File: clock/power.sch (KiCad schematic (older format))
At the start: 50 parts, among them Q501 BSS138, Q502 BSS138, U501 TPS56428, U502 TPS56428, U503 TPS56428

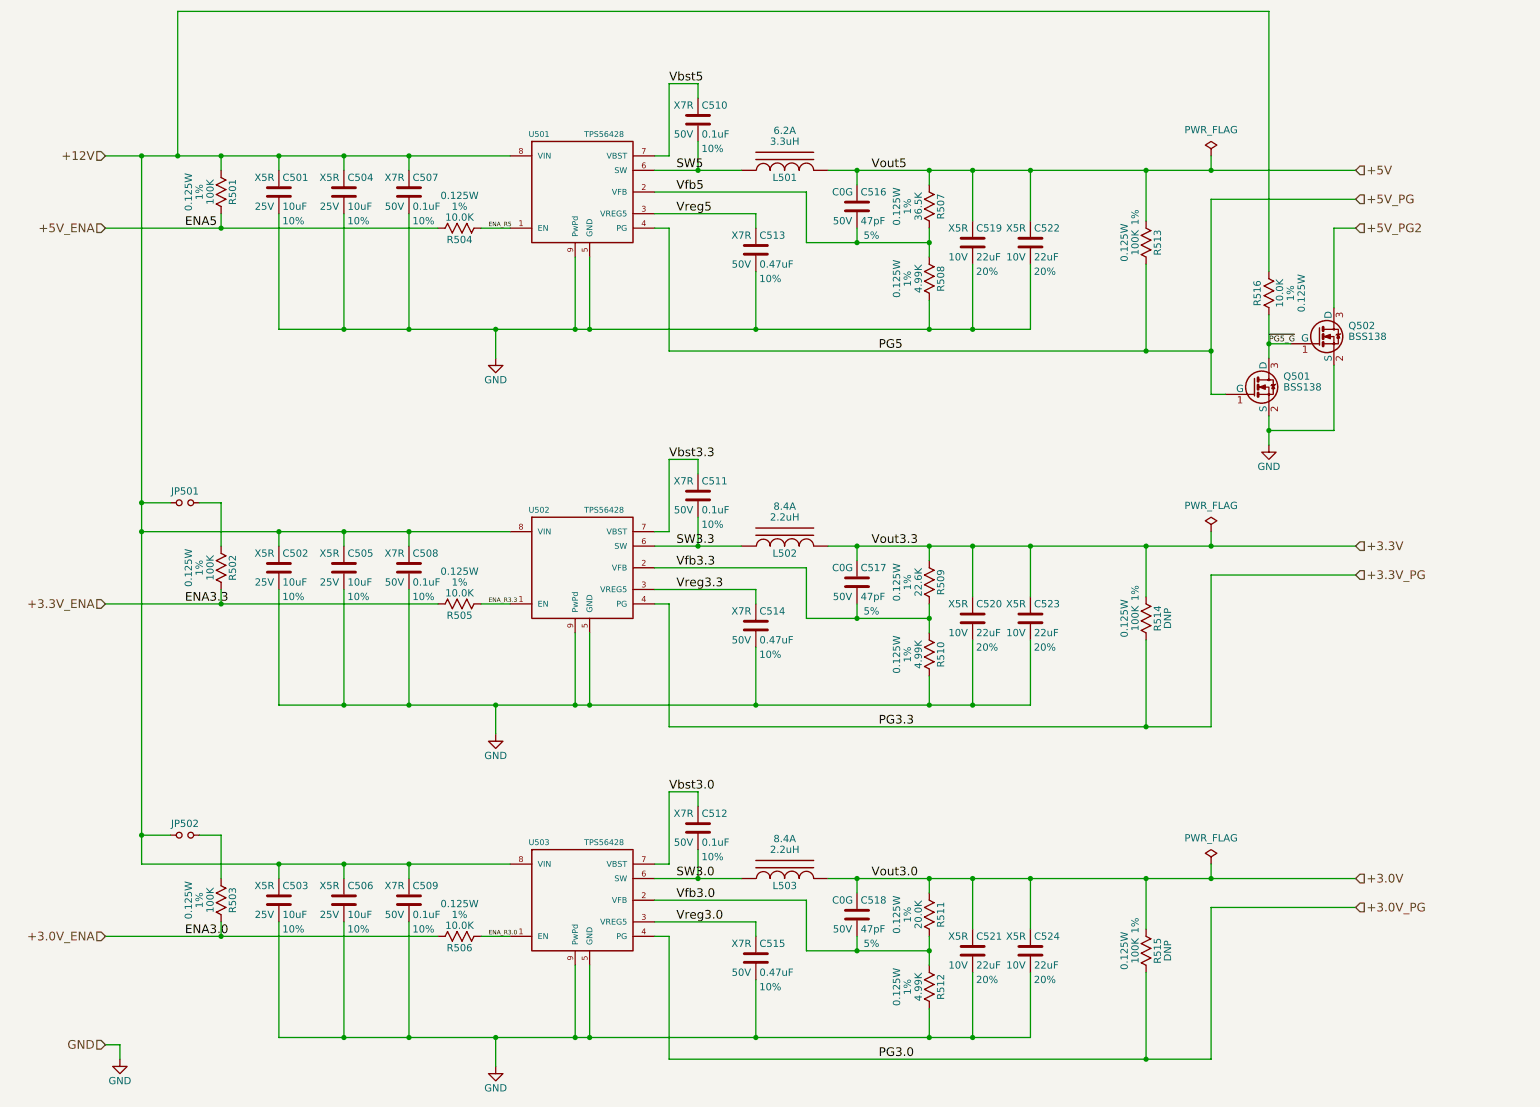
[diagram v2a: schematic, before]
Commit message: Add power indication LEDs.
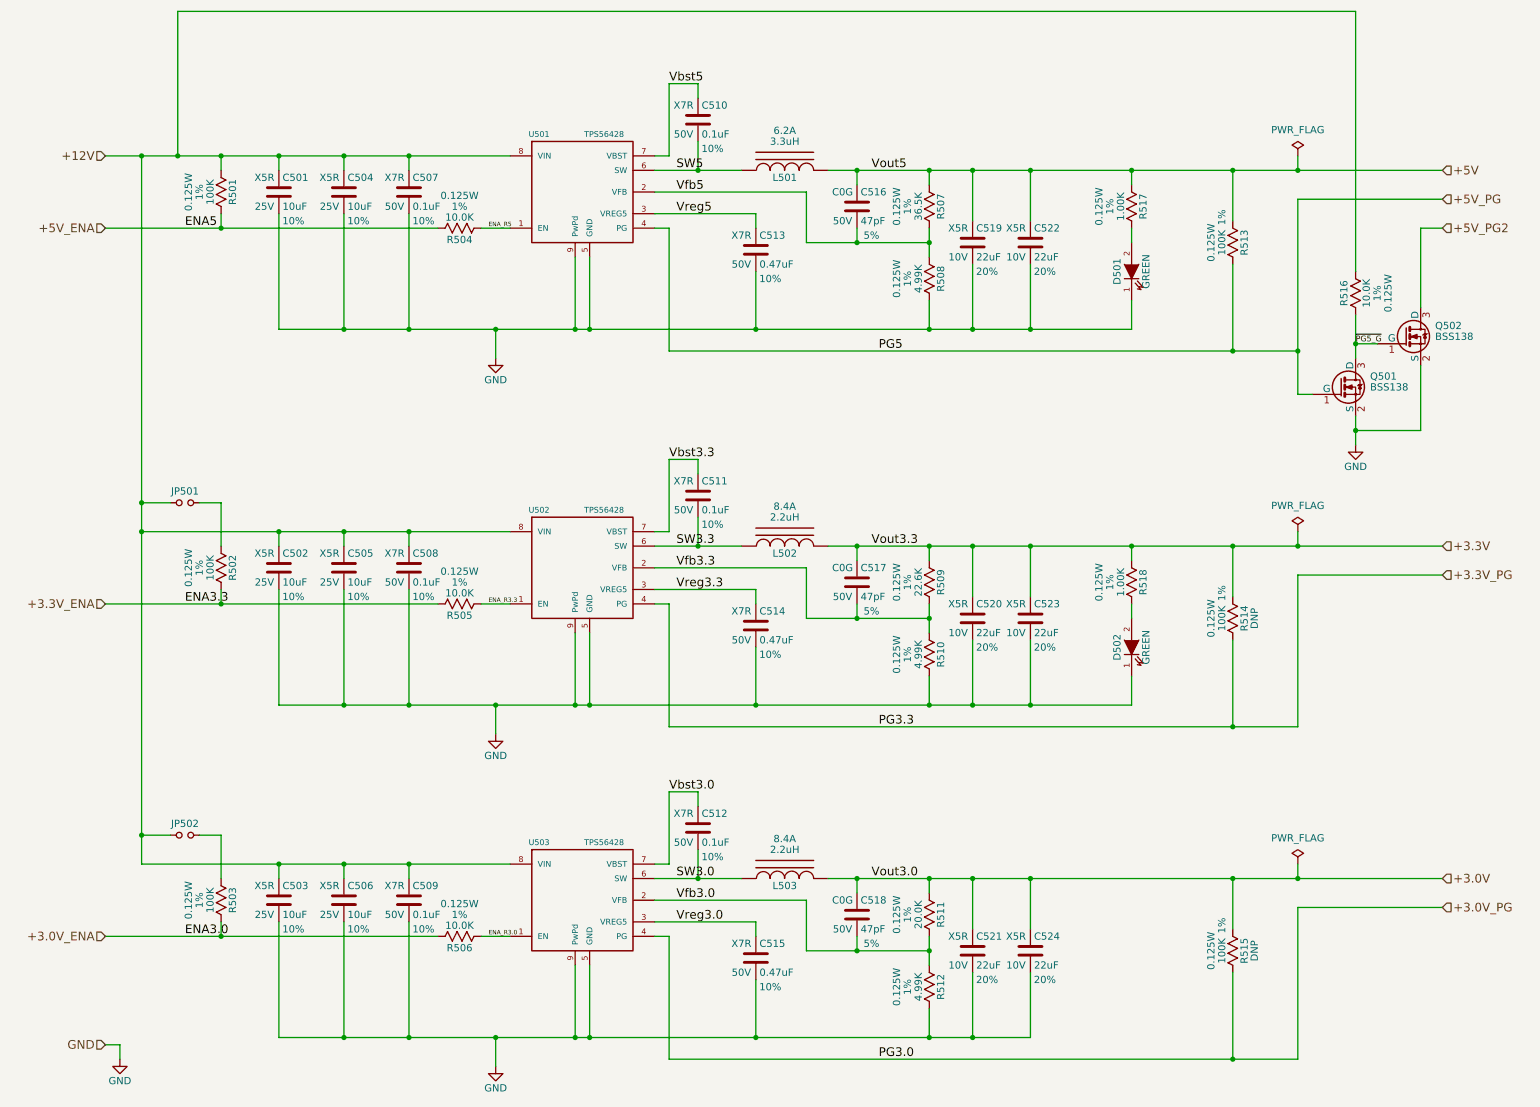
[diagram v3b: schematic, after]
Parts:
- added D501, D502: GREEN, local:LED_0805_HandSoldering, symbol LED
- added R517, R518: 1.00K, local:R_0805_HandSoldering, symbol R_local
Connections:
- net +3.3V: now also R518.1
- net +5V: now also R517.1
- net GND: now also D501.1 (K), D502.1 (K)
- new net: D501.2 (A), R517.2
- new net: D502.2 (A), R518.2
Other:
- moved on the sheet: Q501, Q502, R513, R514, R515, R516

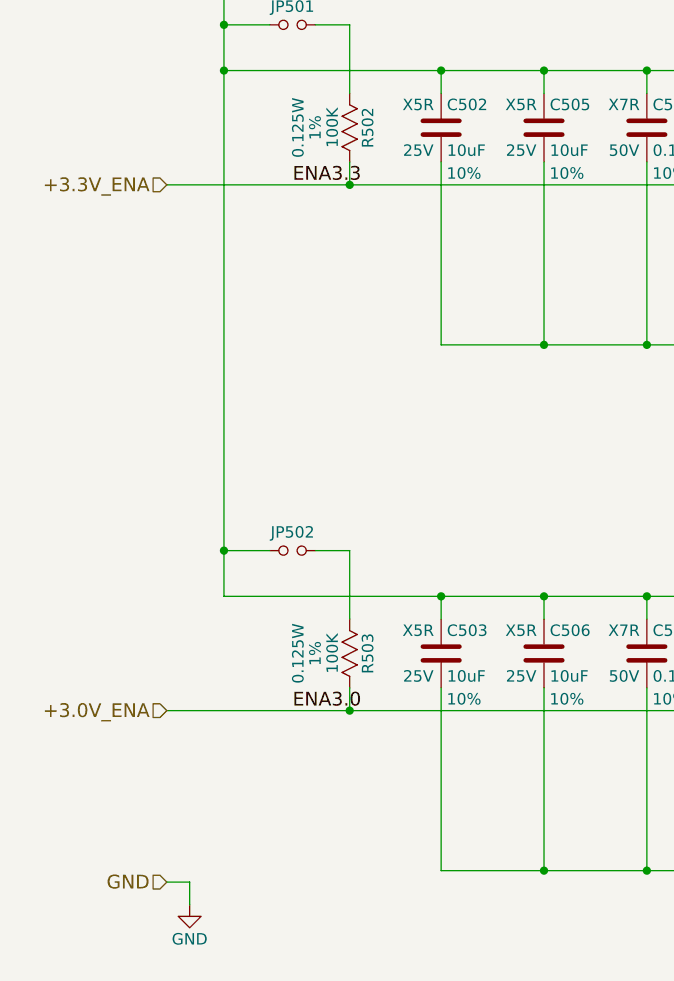
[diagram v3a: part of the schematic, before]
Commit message: Remove sheet to sheet power interconnect because power symbols are global.
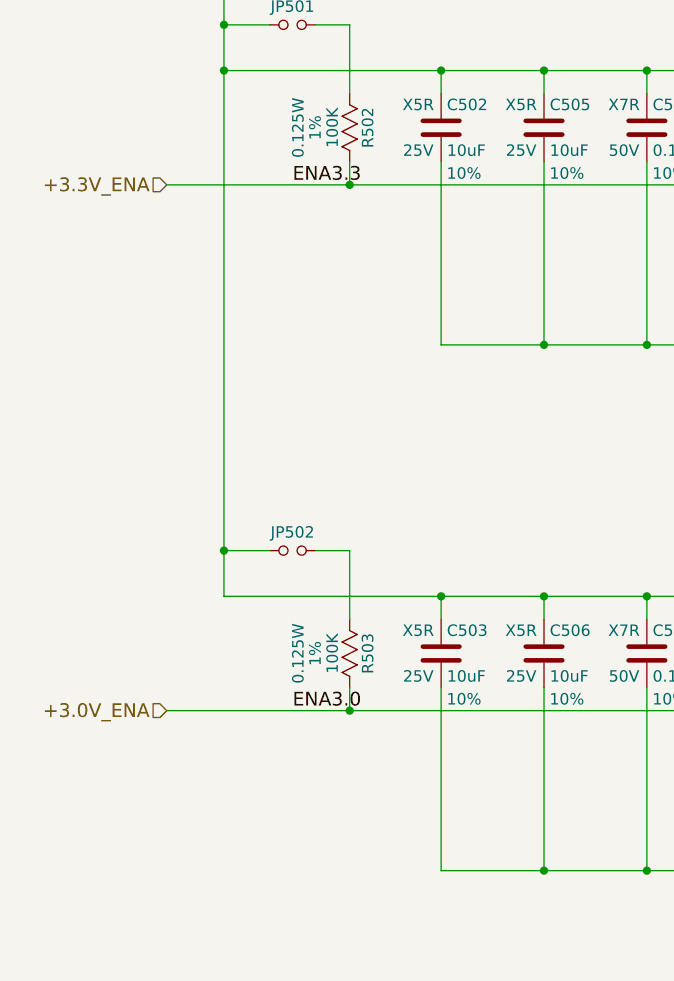
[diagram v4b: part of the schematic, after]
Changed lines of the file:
@@
 Connection ~ 4300 2750
 $Comp
-L GND #PWR502
+L GND #PWR074
 U 1 1 55FF67B4
 P 6200 3650
-F 0 "#PWR502" H 6200 3400 50  0001 C CNN
+F 0 "#PWR074" H 6200 3400 50  0001 C CNN
 F 1 "GND" H 6200 3500 50  0000 C CNN
 F 2 "" H 6200 3650 60  0000 C CNN
@@
 Connection ~ 5150 6050
 Wire Wire Line
-	4700 5250 4700 6050
+	4700 6050 4700 5250
 Wire Wire Line
 	4700 4950 4700 4850
@@
 Connection ~ 4300 5350
 $Comp
-L GND #PWR503
+L GND #PWR075
 U 1 1 5619E4B9
 P 6200 6250
-F 0 "#PWR503" H 6200 6000 50  0001 C CNN
+F 0 "#PWR075" H 6200 6000 50  0001 C CNN
 F 1 "GND" H 6200 6100 50  0000 C CNN
 F 2 "" H 6200 6250 60  0000 C CNN
@@
 Connection ~ 4300 7650
 $Comp
-L GND #PWR504
+L GND #PWR076
 U 1 1 561A0FCA
 P 6200 8550
-F 0 "#PWR504" H 6200 8300 50  0001 C CNN
+F 0 "#PWR076" H 6200 8300 50  0001 C CNN
 F 1 "GND" H 6200 8400 50  0000 C CNN
 F 2 "" H 6200 8550 60  0000 C CNN
@@
 	3950 6950 3750 6950
 Connection ~ 3750 6950
-Text HLabel 3500 8400 0    60   Input ~ 0
-GND
-$Comp
-L GND #PWR501
-U 1 1 563D8E93
-P 3600 8500
-F 0 "#PWR501" H 3600 8250 50  0001 C CNN
-F 1 "GND" H 3600 8350 50  0000 C CNN
-F 2 "" H 3600 8500 60  0000 C CNN
-F 3 "" H 3600 8500 60  0000 C CNN
-	1    3600 8500
-	1    0    0    -1
-$EndComp
-Wire Wire Line
-	3600 8400 3600 8500
-Wire Wire Line
-	3600 8400 3500 8400
-$Comp
-L PWR_FLAG #FLG501
+$Comp
+L PWR_FLAG #FLG077
 U 1 1 56439BF3
 P 11750 2250
-F 0 "#FLG501" H 11750 2345 50  0001 C CNN
+F 0 "#FLG077" H 11750 2345 50  0001 C CNN
 F 1 "PWR_FLAG" H 11750 2430 50  0000 C CNN
 F 2 "" H 11750 2250 60  0000 C CNN
@@
 Connection ~ 11750 2350
 $Comp
-L PWR_FLAG #FLG502
+L PWR_FLAG #FLG078
 U 1 1 5643A4B3
 P 11750 4850
-F 0 "#FLG502" H 11750 4945 50  0001 C CNN
+F 0 "#FLG078" H 11750 4945 50  0001 C CNN
 F 1 "PWR_FLAG" H 11750 5030 50  0000 C CNN
 F 2 "" H 11750 4850 60  0000 C CNN
@@
 Connection ~ 11750 4950
 $Comp
-L PWR_FLAG #FLG503
+L PWR_FLAG #FLG079
 U 1 1 5643AC28
 P 11750 7150
-F 0 "#FLG503" H 11750 7245 50  0001 C CNN
+F 0 "#FLG079" H 11750 7245 50  0001 C CNN
 F 1 "PWR_FLAG" H 11750 7330 50  0000 C CNN
 F 2 "" H 11750 7150 60  0000 C CNN
@@
 	12150 4050 12150 4250
 $Comp
-L GND #PWR505
+L GND #PWR080
 U 1 1 57A97EAC
 P 12150 4250
-F 0 "#PWR505" H 12150 4000 50  0001 C CNN
+F 0 "#PWR080" H 12150 4000 50  0001 C CNN
 F 1 "GND" H 12150 4100 50  0000 C CNN
 F 2 "" H 12150 4250 60  0000 C CNN

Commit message: Update clock board to kicad 5.1. Regenerate output files.
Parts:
- C501, C502, C503, C504, C505, C506, C507, C508, C509, C510, C511, C512, C513, C514, C515, C516, C517, C518, C519, C520, C521, C522, C523, C524: symbol C -> Device:C
- D501, D502: symbol LED -> Local:LED
- JP501, JP502: symbol Jumper_NO_Small -> Jumper:Jumper_2_Open
- L501, L502, L503: symbol L -> Local:L
- Q501, Q502: symbol BSS138 -> Local:BSS138
- R501, R502, R503, R504, R505, R506, R507, R508, R509, R510, R511, R512, R513, R514, R515, R516, R517, R518: symbol R_local -> Local:R_local
- U501, U502, U503: symbol TPS56428 -> Local:TPS56428
